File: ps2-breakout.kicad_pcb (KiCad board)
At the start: 2 copper layers, 33 x 43.2 mm, 34 parts, among them J1 Conn_01x08_Female, J2 Conn_01x08_Female, Q1 MMBF170, Q2 MMBF170, Q3 MMBF170, Q4 MMBF170, U1 RCLAMP0502A, U2 RCLAMP0502A, U3 MD-60SM, U4 MD-60SM

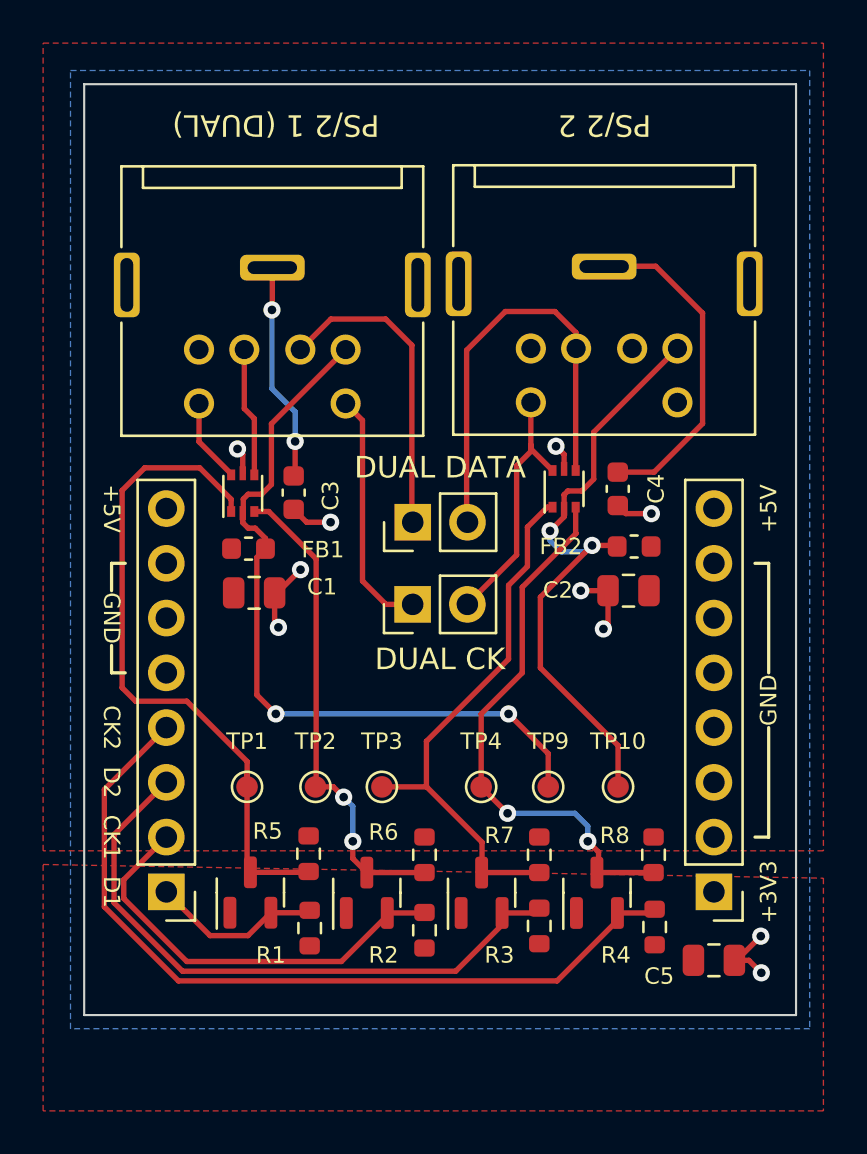
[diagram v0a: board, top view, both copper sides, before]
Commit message: Fix RCLAMP0502 symbol and footprint
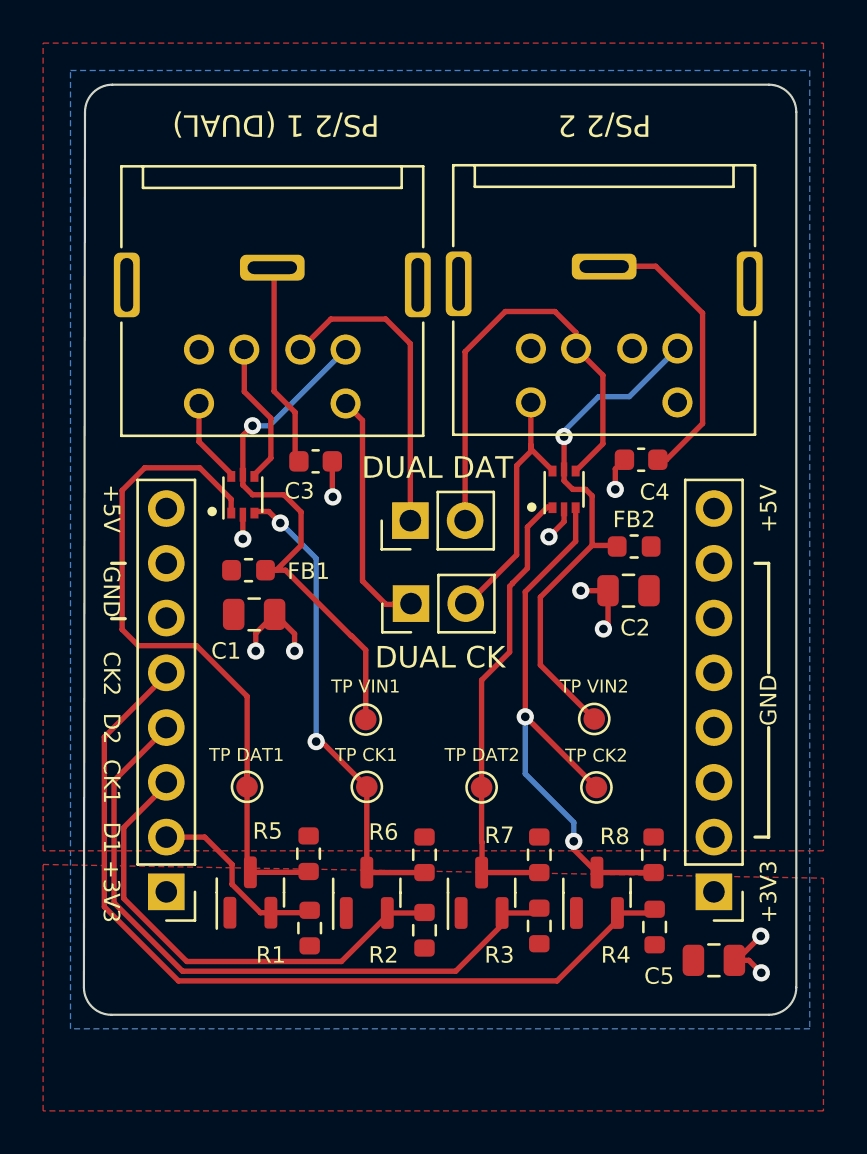
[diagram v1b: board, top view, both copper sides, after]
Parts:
- removed DUAL CK: Jumper_2_Open, Connector_PinHeader_2.54mm:PinHeader_1x02_P2.54mm_Vertical
- removed DUAL DATA: Jumper_2_Open, Connector_PinHeader_2.54mm:PinHeader_1x02_P2.54mm_Vertical
- added DUAL CK1: Jumper_2_Open, Connector_PinHeader_2.54mm:PinHeader_1x02_P2.54mm_Vertical, F.Cu at (113.0, 57.8)
- added DUAL DATA1: Jumper_2_Open, Connector_PinHeader_2.54mm:PinHeader_1x02_P2.54mm_Vertical, F.Cu at (112.9, 53.9)
- moved TP9 9.02 mm to (110.8, 63.1)
- moved TP4 5.35 mm to (121.5, 66.3)
- moved TP3 4.63 mm to (116.2, 66.3)
- moved TP10 3.34 mm to (121.5, 63.1)
- moved G*** 3.17 mm to (111.2, 67.5), turned to 0 degrees
- moved TP2 2.38 mm to (110.9, 66.2)
- moved C3 1.77 mm to (108.5, 51.1), turned to 0 degrees
- moved C4 1.73 mm to (123.6, 51.1), turned to 180 degrees
- moved C1 1.00 mm to (105.7, 58.2)
- moved FB1 1.00 mm to (105.4, 56.2)
- moved U1 0.07 mm to (105.2, 52.7)
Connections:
- J2 pad 1: /PS2_1.DATA -> +3V3
- J2 pad 2: /PS2_1.CLK -> /PS2_1.DATA
- J2 pad 3: /PS2_2.DATA -> /PS2_1.CLK
- J2 pad 4: /PS2_2.CLK -> /PS2_2.DATA
- J2 pad 5: GND -> /PS2_2.CLK
- U1 pad 2: Net-(FB1-Pad2) -> GND
- U1 pad 5: GND -> Net-(FB1-Pad2)
- U2 pad 2: Net-(FB2-Pad2) -> GND
- U2 pad 5: GND -> Net-(FB2-Pad2)
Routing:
- net Net-(FB1-Pad2): track 35.3 -> 24.5 mm, vias 2 -> 1
- net Net-(FB2-Pad2): track 28.9 -> 24.3 mm, vias 2 -> 1
- net Net-(Q3-Pad3): track 25.3 -> 21.1 mm
- net /PS2_2.DATA: track 29.2 -> 31.7 mm
- net /PS2_2.CLK: track 38.0 -> 40.5 mm
- net /PS2_1.CLK: track 19.9 -> 22.3 mm
- net Net-(C4-Pad1): track 15.5 -> 13.4 mm
- net Net-(Q4-Pad3): track 25.5 -> 26.6 mm
- net /PS2_2.DATA_PIN_1: track 20.6 -> 21.6 mm
- net /PS2_1.DATA: track 8.03 -> 8.74 mm
- net Net-(U1-Pad4): track 6.00 -> 6.71 mm
- net Net-(C3-Pad1): track 10.1 -> 9.50 mm, vias 2 -> 0
- net GND: track 15.7 -> 16.4 mm
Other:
- board size 33 x 43.2 mm -> 33 x 43.1 mm
- board text added: "DUAL CK"
- board text added: "DUAL DAT"
- board text added: "TP CK1"
- board text added: "TP CK2"
- board text added: "TP DAT1"
- board text added: "TP DAT2"
- board text added: "TP VIN1"
- board text added: "TP VIN2"
